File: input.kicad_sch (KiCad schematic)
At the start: 11 parts, among them J3 5077CR-16SMC2-BK-TR, J4 MainBattery, J5 SubBattery

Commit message: update pcb
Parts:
- removed J4: MainBattery, Connector_JST:JST_XA_B02B-XASK-1_1x02_P2.50mm_Vertical, symbol Connector_Generic:Conn_01x02
- removed J5: SubBattery, Connector_JST:JST_XA_B02B-XASK-1_1x02_P2.50mm_Vertical, symbol Connector_Generic:Conn_01x02
- added D3: DF2S232CTC, Diode_SMD:D_0603_1608Metric_Pad1.05x0.95mm_HandSolder, symbol Device:D_Schottky_Filled
- added J1: MainBattery, Connector_JST:JST_XA_B03B-XASK-1_1x03_P2.50mm_Vertical, symbol Connector_Generic:Conn_01x03
- added J3: SubBattery, Connector_JST:JST_XA_B03B-XASK-1_1x03_P2.50mm_Vertical, symbol Connector_Generic:Conn_01x03
- renumbered C31 to C24, C26 to C25, C30 to C26, D2 to D4, J3 to J2, R4 to R17, R8 to R18, R7 to R19, TP1 to TP3
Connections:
- net GND: now also D3.2 (A), J1.1 (Pin_1), J3.1 (Pin_1)
- net Main-Bat: now also J1.3 (Pin_3)
- net VBUS: now also D3.1 (K)
- net V_{OUT}2: now also J3.3 (Pin_3)
- new net NTC1: J1.2 (Pin_2)
- new net NTC2: J3.2 (Pin_2)
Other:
- moved on the sheet: C24, C25, C26

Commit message: update pcb ltc4088kitsui
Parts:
- C2: renamed from C25; value 100u -> 10u; footprint Capacitor_SMD:C_1206_3216Metric_Pad1.33x1.80mm_HandSolder -> Capacitor_SMD:C_0805_2012Metric_Pad1.18x1.45mm_HandSolder
- renumbered C24 to C1, C26 to C3, D3 to D1, D4 to D2, R17 to R1, R18 to R2, R19 to R3
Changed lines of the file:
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@@
 		(dnp no)
 		(fields_autoplaced yes)
-		(property "Reference" "#PWR038"
+		(property "Reference" "#PWR012"
 			(at 231.14 81.28 0)
 			(effects
@@
 			(project "Avio-BMS"
 				(path "/14e0994b-afc2-4c10-b50d-3efcc006980d/a9aee824-ba4d-405a-8d21-1d0bdb676b29"
-					(reference "#PWR038")
+					(reference "#PWR012")
 					(unit 1)
 				)
@@
 		(dnp no)
 		(fields_autoplaced yes)
-		(property "Reference" "#PWR037"
+		(property "Reference" "#PWR011"
 			(at 222.25 118.11 0)
 			(effects
@@
 			(project "Avio-BMS"
 				(path "/14e0994b-afc2-4c10-b50d-3efcc006980d/a9aee824-ba4d-405a-8d21-1d0bdb676b29"
-					(reference "#PWR037")
+					(reference "#PWR011")
 					(unit 1)
 				)
@@
 		(dnp no)
 		(fields_autoplaced yes)
-		(property "Reference" "#PWR029"
+		(property "Reference" "#PWR03"
 			(at 93.98 86.36 0)
 			(effects
@@
 			(project "Avio-BMS"
 				(path "/14e0994b-afc2-4c10-b50d-3efcc006980d/a9aee824-ba4d-405a-8d21-1d0bdb676b29"
-					(reference "#PWR029")
+					(reference "#PWR03")
 					(unit 1)
 				)
@@
 		(dnp no)
 		(fields_autoplaced yes)
-		(property "Reference" "#PWR034"
+		(property "Reference" "#PWR08"
 			(at 152.4 93.98 0)
 			(effects
@@
 			(project "Avio-BMS"
 				(path "/14e0994b-afc2-4c10-b50d-3efcc006980d/a9aee824-ba4d-405a-8d21-1d0bdb676b29"
-					(reference "#PWR034")
+					(reference "#PWR08")
 					(unit 1)
 				)
@@
 		(dnp no)
 		(fields_autoplaced yes)
-		(property "Reference" "#PWR033"
+		(property "Reference" "#PWR07"
 			(at 147.32 99.06 0)
 			(effects
@@
 			(project "Avio-BMS"
 				(path "/14e0994b-afc2-4c10-b50d-3efcc006980d/a9aee824-ba4d-405a-8d21-1d0bdb676b29"
-					(reference "#PWR033")
+					(reference "#PWR07")
 					(unit 1)
 				)
@@
 		(on_board yes)
 		(dnp no)
-		(property "Reference" "D3"
+		(property "Reference" "D1"
 			(at 160.02 84.7724 90)
 			(effects
@@
 			(project ""
 				(path "/14e0994b-afc2-4c10-b50d-3efcc006980d/a9aee824-ba4d-405a-8d21-1d0bdb676b29"
-					(reference "D3")
+					(reference "D1")
 					(unit 1)
 				)
@@
 		(on_board yes)
 		(dnp no)
-		(property "Reference" "R17"
+		(property "Reference" "R1"
 			(at 102.362 84.582 90)
 			(effects
@@
 			(project "Avio-BMS"
 				(path "/14e0994b-afc2-4c10-b50d-3efcc006980d/a9aee824-ba4d-405a-8d21-1d0bdb676b29"
-					(reference "R17")
+					(reference "R1")
 					(unit 1)
 				)
@@
 		(dnp no)
 		(fields_autoplaced yes)
-		(property "Reference" "#PWR036"
+		(property "Reference" "#PWR010"
 			(at 203.2 102.87 0)
 			(effects
@@
 			(project "Avio-BMS"
 				(path "/14e0994b-afc2-4c10-b50d-3efcc006980d/a9aee824-ba4d-405a-8d21-1d0bdb676b29"
-					(reference "#PWR036")
+					(reference "#PWR010")
 					(unit 1)
 				)
@@
 		(dnp no)
 		(fields_autoplaced yes)
-		(property "Reference" "#PWR035"
+		(property "Reference" "#PWR09"
 			(at 157.48 97.79 0)
 			(effects
@@
 			(project "Avio-BMS"
 				(path "/14e0994b-afc2-4c10-b50d-3efcc006980d/a9aee824-ba4d-405a-8d21-1d0bdb676b29"
-					(reference "#PWR035")
+					(reference "#PWR09")
 					(unit 1)
 				)
@@
 		(dnp no)
 		(fields_autoplaced yes)
-		(property "Reference" "C25"
+		(property "Reference" "C2"
 			(at 193.04 83.8199 0)
 			(effects
@@
 			)
 		)
-		(property "Value" "100u"
+		(property "Value" "10u"
 			(at 193.04 86.3599 0)
 			(effects
@@
 			)
 		)
-		(property "Footprint" "Capacitor_SMD:C_1206_3216Metric_Pad1.33x1.80mm_HandSolder"
+		(property "Footprint" "Capacitor_SMD:C_0805_2012Metric_Pad1.18x1.45mm_HandSolder"
 			(at 190.1952 88.9 0)
 			(effects
@@
 			(project ""
 				(path "/14e0994b-afc2-4c10-b50d-3efcc006980d/a9aee824-ba4d-405a-8d21-1d0bdb676b29"
-					(reference "C25")
+					(reference "C2")
 					(unit 1)
 				)
@@
 		(on_board yes)
 		(dnp no)
-		(property "Reference" "D4"
+		(property "Reference" "D2"
 			(at 218.948 99.314 90)
 			(effects
@@
 			(project "Avio-BMS"
 				(path "/14e0994b-afc2-4c10-b50d-3efcc006980d/a9aee824-ba4d-405a-8d21-1d0bdb676b29"
-					(reference "D4")
+					(reference "D2")
 					(unit 1)
 				)
@@
 		(dnp no)
 		(fields_autoplaced yes)
-		(property "Reference" "#PWR032"
+		(property "Reference" "#PWR06"
 			(at 133.35 132.08 0)
 			(effects
@@
 			(project "Avio-BMS"
 				(path "/14e0994b-afc2-4c10-b50d-3efcc006980d/a9aee824-ba4d-405a-8d21-1d0bdb676b29"
-					(reference "#PWR032")
+					(reference "#PWR06")
 					(unit 1)
 				)
@@
 		(dnp no)
 		(fields_autoplaced yes)
-		(property "Reference" "C26"
+		(property "Reference" "C3"
 			(at 207.01 83.8199 0)
 			(effects
@@
 			(project "Avio-BMS"
 				(path "/14e0994b-afc2-4c10-b50d-3efcc006980d/a9aee824-ba4d-405a-8d21-1d0bdb676b29"
-					(reference "C26")
+					(reference "C3")
 					(unit 1)
 				)
@@
 		(dnp no)
 		(fields_autoplaced yes)
-		(property "Reference" "#PWR031"
+		(property "Reference" "#PWR05"
 			(at 143.51 127 0)
 			(effects
@@
 			(project "Avio-BMS"
 				(path "/14e0994b-afc2-4c10-b50d-3efcc006980d/a9aee824-ba4d-405a-8d21-1d0bdb676b29"
-					(reference "#PWR031")
+					(reference "#PWR05")
 					(unit 1)
 				)
@@
 		(dnp no)
 		(fields_autoplaced yes)
-		(property "Reference" "C24"
+		(property "Reference" "C1"
 			(at 177.8 83.8262 0)
 			(effects
@@
 			(project ""
 				(path "/14e0994b-afc2-4c10-b50d-3efcc006980d/a9aee824-ba4d-405a-8d21-1d0bdb676b29"
-					(reference "C24")
+					(reference "C1")
 					(unit 1)
 				)
@@
 		(dnp no)
 		(fields_autoplaced yes)
-		(property "Reference" "#PWR030"
+		(property "Reference" "#PWR04"
 			(at 105.41 132.08 0)
 			(effects
@@
 			(project "Avio-BMS"
 				(path "/14e0994b-afc2-4c10-b50d-3efcc006980d/a9aee824-ba4d-405a-8d21-1d0bdb676b29"
-					(reference "#PWR030")
+					(reference "#PWR04")
 					(unit 1)
 				)
@@
 		(on_board yes)
 		(dnp no)
-		(property "Reference" "R19"
+		(property "Reference" "R3"
 			(at 220.472 90.17 0)
 			(effects
@@
 			(project "Avio-BMS"
 				(path "/14e0994b-afc2-4c10-b50d-3efcc006980d/a9aee824-ba4d-405a-8d21-1d0bdb676b29"
-					(reference "R19")
+					(reference "R3")
 					(unit 1)
 				)
@@
 		(on_board yes)
 		(dnp no)
-		(property "Reference" "R18"
+		(property "Reference" "R2"
 			(at 143.764 92.202 90)
 			(effects
@@
 			(project "Avio-BMS"
 				(path "/14e0994b-afc2-4c10-b50d-3efcc006980d/a9aee824-ba4d-405a-8d21-1d0bdb676b29"
-					(reference "R18")
-					(unit 1)
-				)
+					(reference "R2")
+					(unit 1)
+				)

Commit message: update pcb
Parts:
- removed C1: OPT1608, Capacitor_SMD:C_0603_1608Metric_Pad1.08x0.95mm_HandSolder, symbol Device:C_Small
- removed C3: OPT3216, Capacitor_SMD:C_1206_3216Metric_Pad1.33x1.80mm_HandSolder, symbol Device:C
- added C1: 10u, Capacitor_SMD:C_0805_2012Metric_Pad1.18x1.45mm_HandSolder, symbol Device:C
- added R27: 10M, Resistor_SMD:R_0603_1608Metric_Pad0.98x0.95mm_HandSolder, symbol Device:R_Small
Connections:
- net GND: now also C1.2, R27.1
- net at J2.S1 (SHIELD), J2.S2 (SHIELD), J2.S3 (SHIELD)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: now also C1.1, R27.2
- no-connect marks 0 -> 6
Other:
- moved on the sheet: C2, D2, R3

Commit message: ad datasheet
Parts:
- renumbered R27 to R1, R1 to R2, R2 to R3, R3 to R4
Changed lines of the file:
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@@
+		(dnp no)
+		(fields_autoplaced yes)
+		(property "Reference" "#PWR013"
+			(at 231.14 81.28 0)
+			(effects
+				(font
+					(size 1.27 1.27)
+				)
+				(hide yes)
+			)
+		)
+		(property "Value" "VBUS"
+			(at 238.76 81.2799 90)
+			(effects
+				(font
+					(size 1.27 1.27)
+				)
+				(justify left)
+			)
+		)
+		(property "Footprint" ""
+			(at 234.95 81.28 0)
+			(effects
+				(font
+					(size 1.27 1.27)
+				)
+				(hide yes)
+			)
+		)
+		(property "Datasheet" ""
+			(at 234.95 81.28 0)
+			(effects
+				(font
+					(size 1.27 1.27)
+				)
+				(hide yes)
+			)
+		)
+		(property "Description" "Power symbol creates a global label with name \"VBUS\""
+			(at 234.95 81.28 0)
+			(effects
+				(font
+					(size 1.27 1.27)
+				)
+				(hide yes)
+			)
+		)
+		(pin "1"
+		)
+		(instances
+			(project "Avio-BMS"
+				(path "/14e0994b-afc2-4c10-b50d-3efcc006980d/a9aee824-ba4d-405a-8d21-1d0bdb676b29"
+					(reference "#PWR013")
+					(unit 1)
+				)
+			)
+		)
+	)
+	(symbol
+		(lib_id "power:GND")
+		(at 214.63 111.76 0)
+		(unit 1)
+		(exclude_from_sim no)
+		(in_bom yes)
+		(on_board yes)
 		(dnp no)
 		(fields_autoplaced yes)
 		(property "Reference" "#PWR012"
-			(at 231.14 81.28 0)
-			(effects
-				(font
-					(size 1.27 1.27)
-				)
-				(hide yes)
-			)
-		)
-		(property "Value" "VBUS"
-			(at 238.76 81.2799 90)
-			(effects
-				(font
-					(size 1.27 1.27)
-				)
-				(justify left)
-			)
-		)
-		(property "Footprint" ""
-			(at 234.95 81.28 0)
-			(effects
-				(font
-					(size 1.27 1.27)
-				)
-				(hide yes)
-			)
-		)
-		(property "Datasheet" ""
-			(at 234.95 81.28 0)
-			(effects
-				(font
-					(size 1.27 1.27)
-				)
-				(hide yes)
-			)
-		)
-		(property "Description" "Power symbol creates a global label with name \"VBUS\""
-			(at 234.95 81.28 0)
-			(effects
-				(font
-					(size 1.27 1.27)
-				)
-				(hide yes)
-			)
-		)
-		(pin "1"
-		)
-		(instances
-			(project "Avio-BMS"
-				(path "/14e0994b-afc2-4c10-b50d-3efcc006980d/a9aee824-ba4d-405a-8d21-1d0bdb676b29"
-					(reference "#PWR012")
-					(unit 1)
-				)
-			)
-		)
-	)
-	(symbol
-		(lib_id "power:GND")
-		(at 214.63 111.76 0)
-		(unit 1)
-		(exclude_from_sim no)
-		(in_bom yes)
-		(on_board yes)
-		(dnp no)
-		(fields_autoplaced yes)
-		(property "Reference" "#PWR011"
 			(at 214.63 118.11 0)
 			(effects
@@
 			(project "Avio-BMS"
 				(path "/14e0994b-afc2-4c10-b50d-3efcc006980d/a9aee824-ba4d-405a-8d21-1d0bdb676b29"
-					(reference "#PWR011")
+					(reference "#PWR012")
 					(unit 1)
 				)
@@
 		(dnp no)
 		(fields_autoplaced yes)
-		(property "Reference" "#PWR03"
+		(property "Reference" "#PWR04"
 			(at 93.98 86.36 0)
 			(effects
@@
 			(project "Avio-BMS"
 				(path "/14e0994b-afc2-4c10-b50d-3efcc006980d/a9aee824-ba4d-405a-8d21-1d0bdb676b29"
-					(reference "#PWR03")
+					(reference "#PWR04")
 					(unit 1)
 				)
@@
 		(dnp no)
 		(fields_autoplaced yes)
-		(property "Reference" "#PWR08"
+		(property "Reference" "#PWR09"
 			(at 152.4 93.98 0)
 			(effects
@@
 			(project "Avio-BMS"
 				(path "/14e0994b-afc2-4c10-b50d-3efcc006980d/a9aee824-ba4d-405a-8d21-1d0bdb676b29"
-					(reference "#PWR08")
+					(reference "#PWR09")
 					(unit 1)
 				)
@@
 		(dnp no)
 		(fields_autoplaced yes)
-		(property "Reference" "#PWR07"
+		(property "Reference" "#PWR08"
 			(at 147.32 99.06 0)
 			(effects
@@
 			(project "Avio-BMS"
 				(path "/14e0994b-afc2-4c10-b50d-3efcc006980d/a9aee824-ba4d-405a-8d21-1d0bdb676b29"
-					(reference "#PWR07")
+					(reference "#PWR08")
 					(unit 1)
 				)
@@
 		(on_board yes)
 		(dnp no)
-		(property "Reference" "R1"
+		(property "Reference" "R2"
 			(at 102.362 84.582 90)
 			(effects
@@
 			(project "Avio-BMS"
 				(path "/14e0994b-afc2-4c10-b50d-3efcc006980d/a9aee824-ba4d-405a-8d21-1d0bdb676b29"
-					(reference "R1")
+					(reference "R2")
 					(unit 1)
 				)
@@
 		(dnp no)
 		(fields_autoplaced yes)
-		(property "Reference" "#PWR010"
+		(property "Reference" "#PWR011"
 			(at 189.23 100.33 0)
 			(effects
@@
 			(project "Avio-BMS"
 				(path "/14e0994b-afc2-4c10-b50d-3efcc006980d/a9aee824-ba4d-405a-8d21-1d0bdb676b29"
-					(reference "#PWR010")
+					(reference "#PWR011")
 					(unit 1)
 				)
@@
 		(dnp no)
 		(fields_autoplaced yes)
-		(property "Reference" "#PWR09"
+		(property "Reference" "#PWR010"
 			(at 157.48 97.79 0)
 			(effects
@@
 			(project "Avio-BMS"
 				(path "/14e0994b-afc2-4c10-b50d-3efcc006980d/a9aee824-ba4d-405a-8d21-1d0bdb676b29"
-					(reference "#PWR09")
+					(reference "#PWR010")
 					(unit 1)
 				)
@@
 		(on_board yes)
 		(dnp no)
-		(property "Reference" "R27"
+		(property "Reference" "R1"
 			(at 92.202 102.616 0)
 			(effects
@@
 			(project "Avio-BMS"
 				(path "/14e0994b-afc2-4c10-b50d-3efcc006980d/a9aee824-ba4d-405a-8d21-1d0bdb676b29"
-					(reference "R27")
+					(reference "R1")
 					(unit 1)
 				)
@@
 		(dnp no)
 		(fields_autoplaced yes)
-		(property "Reference" "#PWR050"
+		(property "Reference" "#PWR03"
 			(at 95.25 118.11 0)
 			(effects
@@
 			(project "Avio-BMS"
 				(path "/14e0994b-afc2-4c10-b50d-3efcc006980d/a9aee824-ba4d-405a-8d21-1d0bdb676b29"
-					(reference "#PWR050")
+					(reference "#PWR03")
 					(unit 1)
 				)
@@
 		(dnp no)
 		(fields_autoplaced yes)
-		(property "Reference" "#PWR06"
+		(property "Reference" "#PWR07"
 			(at 133.35 132.08 0)
 			(effects
@@
 			(project "Avio-BMS"
 				(path "/14e0994b-afc2-4c10-b50d-3efcc006980d/a9aee824-ba4d-405a-8d21-1d0bdb676b29"
-					(reference "#PWR06")
+					(reference "#PWR07")
 					(unit 1)
 				)
@@
 		(dnp no)
 		(fields_autoplaced yes)
-		(property "Reference" "#PWR05"
+		(property "Reference" "#PWR06"
 			(at 143.51 127 0)
 			(effects
@@
 			(project "Avio-BMS"
 				(path "/14e0994b-afc2-4c10-b50d-3efcc006980d/a9aee824-ba4d-405a-8d21-1d0bdb676b29"
-					(reference "#PWR05")
+					(reference "#PWR06")
 					(unit 1)
 				)
@@
 		(dnp no)
 		(fields_autoplaced yes)
-		(property "Reference" "#PWR04"
+		(property "Reference" "#PWR05"
 			(at 105.41 132.08 0)
 			(effects
@@
 			(project "Avio-BMS"
 				(path "/14e0994b-afc2-4c10-b50d-3efcc006980d/a9aee824-ba4d-405a-8d21-1d0bdb676b29"
-					(reference "#PWR04")
+					(reference "#PWR05")
 					(unit 1)
 				)
@@
 		(on_board yes)
 		(dnp no)
-		(property "Reference" "R3"
+		(property "Reference" "R4"
 			(at 212.852 90.17 0)
 			(effects
@@
 			(project "Avio-BMS"
 				(path "/14e0994b-afc2-4c10-b50d-3efcc006980d/a9aee824-ba4d-405a-8d21-1d0bdb676b29"
-					(reference "R3")
+					(reference "R4")
 					(unit 1)
 				)
@@
 		(on_board yes)
 		(dnp no)
-		(property "Reference" "R2"
+		(property "Reference" "R3"
 			(at 143.764 92.202 90)
 			(effects
@@
 			(project "Avio-BMS"
 				(path "/14e0994b-afc2-4c10-b50d-3efcc006980d/a9aee824-ba4d-405a-8d21-1d0bdb676b29"
-					(reference "R2")
-					(unit 1)
-				)
+					(reference "R3")
+					(unit 1)
+				)

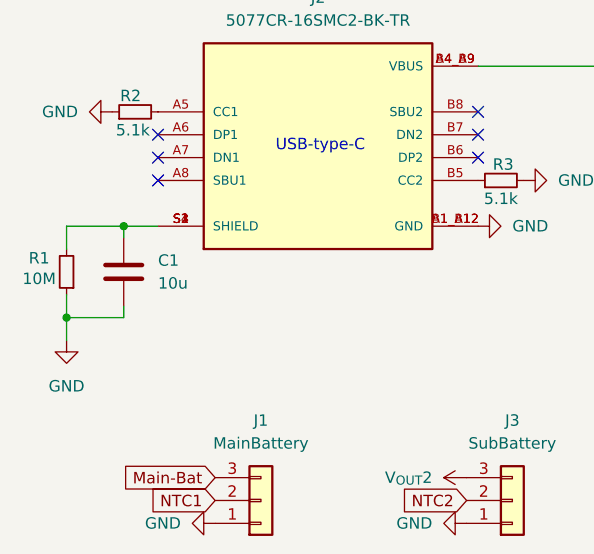
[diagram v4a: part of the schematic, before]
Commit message: remove autosave and lock files; update component values and footprints; add new drill and Gerber files; create BOM
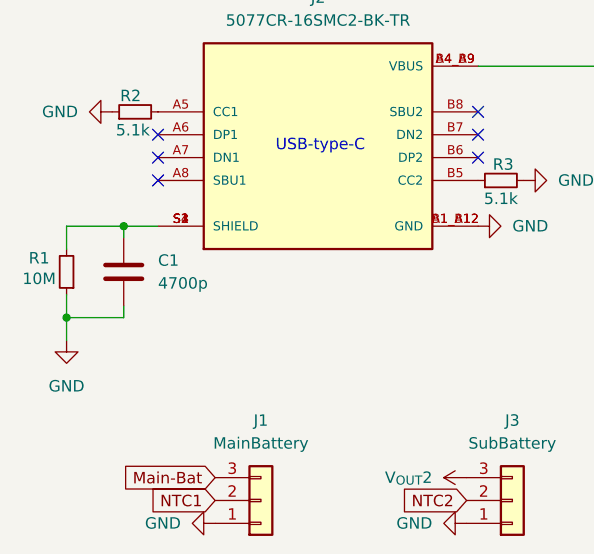
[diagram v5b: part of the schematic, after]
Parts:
- C1: value 10u -> 4700p; footprint Capacitor_SMD:C_0805_2012Metric_Pad1.18x1.45mm_HandSolder -> Capacitor_SMD:C_1206_3216Metric_Pad1.33x1.80mm_HandSolder
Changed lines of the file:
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@@
 			)
 		)
-		(property "Value" "10u"
+		(property "Value" "4700p"
 			(at 105.41 105.4099 0)
 			(effects
@@
 			)
 		)
-		(property "Footprint" "Capacitor_SMD:C_0805_2012Metric_Pad1.18x1.45mm_HandSolder"
+		(property "Footprint" "Capacitor_SMD:C_1206_3216Metric_Pad1.33x1.80mm_HandSolder"
 			(at 102.5652 107.95 0)
 			(effects

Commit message: update sch
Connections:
- net V_{OUT}2 renamed Sub-Bat
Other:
- moved on the sheet: J1, J3

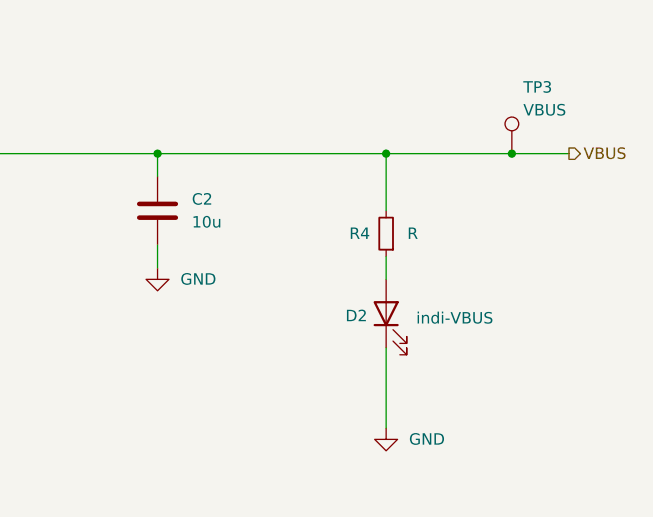
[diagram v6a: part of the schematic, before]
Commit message: 値の更新とテキストボックスの修正; LTC4088およびLTC4417の新しいテキスト追加
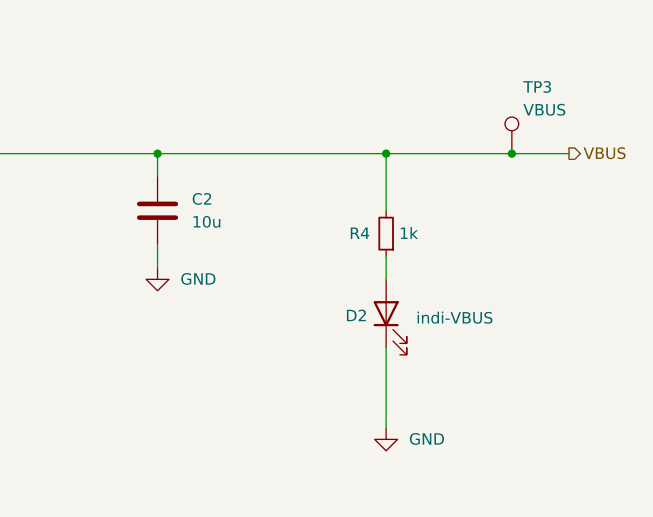
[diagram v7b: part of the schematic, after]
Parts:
- R4: value R -> 1k
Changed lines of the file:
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@@
 			)
 		)
-		(property "Value" "R"
+		(property "Value" "1k"
 			(at 218.186 90.17 0)
 			(effects
